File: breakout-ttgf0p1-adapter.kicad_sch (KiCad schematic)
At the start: 47 parts, among them J1 Conn_01x12, J2 Conn_02x08_Odd_Even, J3 DF12NB-60DS-0.5V_51, J4 Conn_02x08_Odd_Even, J5 DF12NB-50DS-0.5V_51, J6 Conn_02x08_Odd_Even, J8 Conn_02x08_Odd_Even, U1 AP2112K-3.3, U2 AP2112K-3.3, U4 24LC02

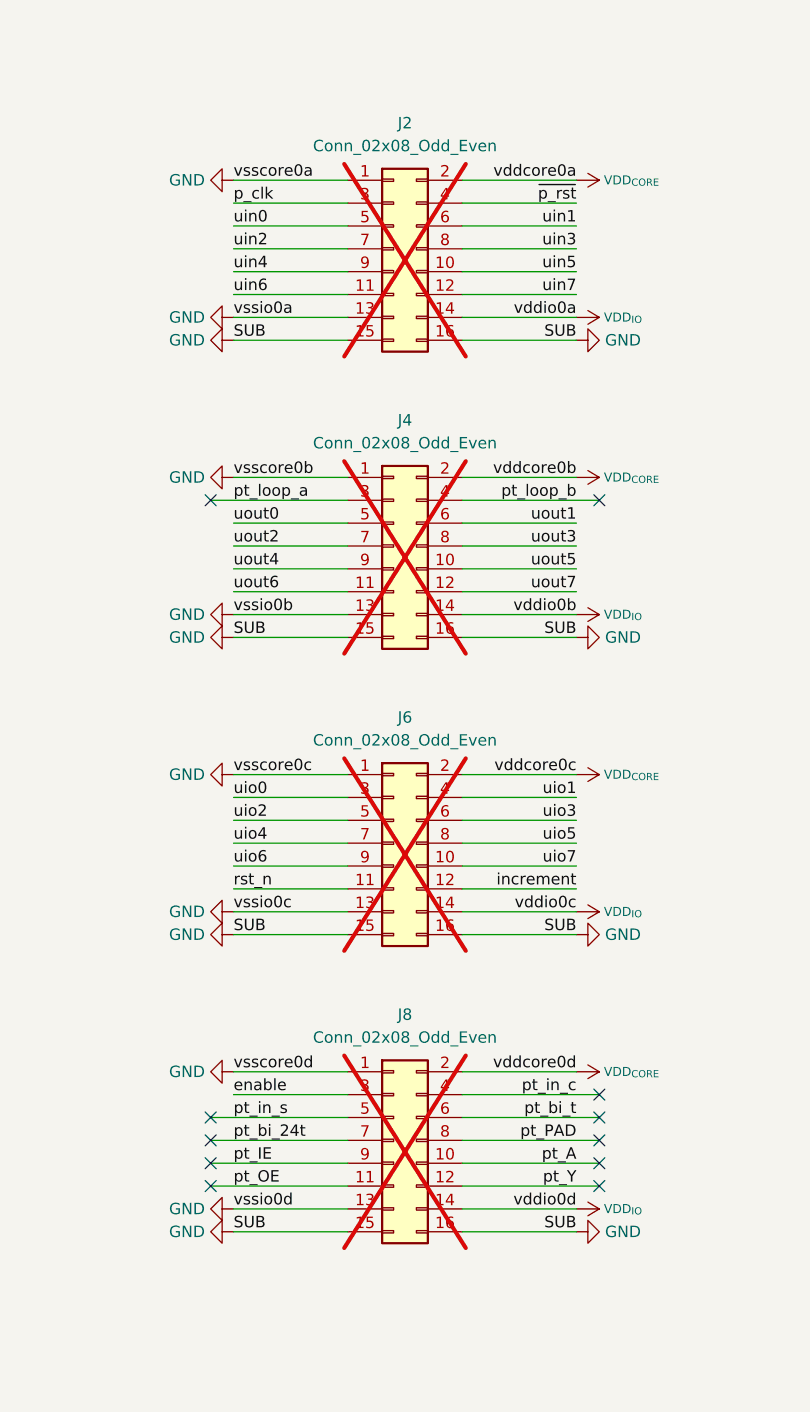
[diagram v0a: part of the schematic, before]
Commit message: replace THT headers with SMT ones & reroute
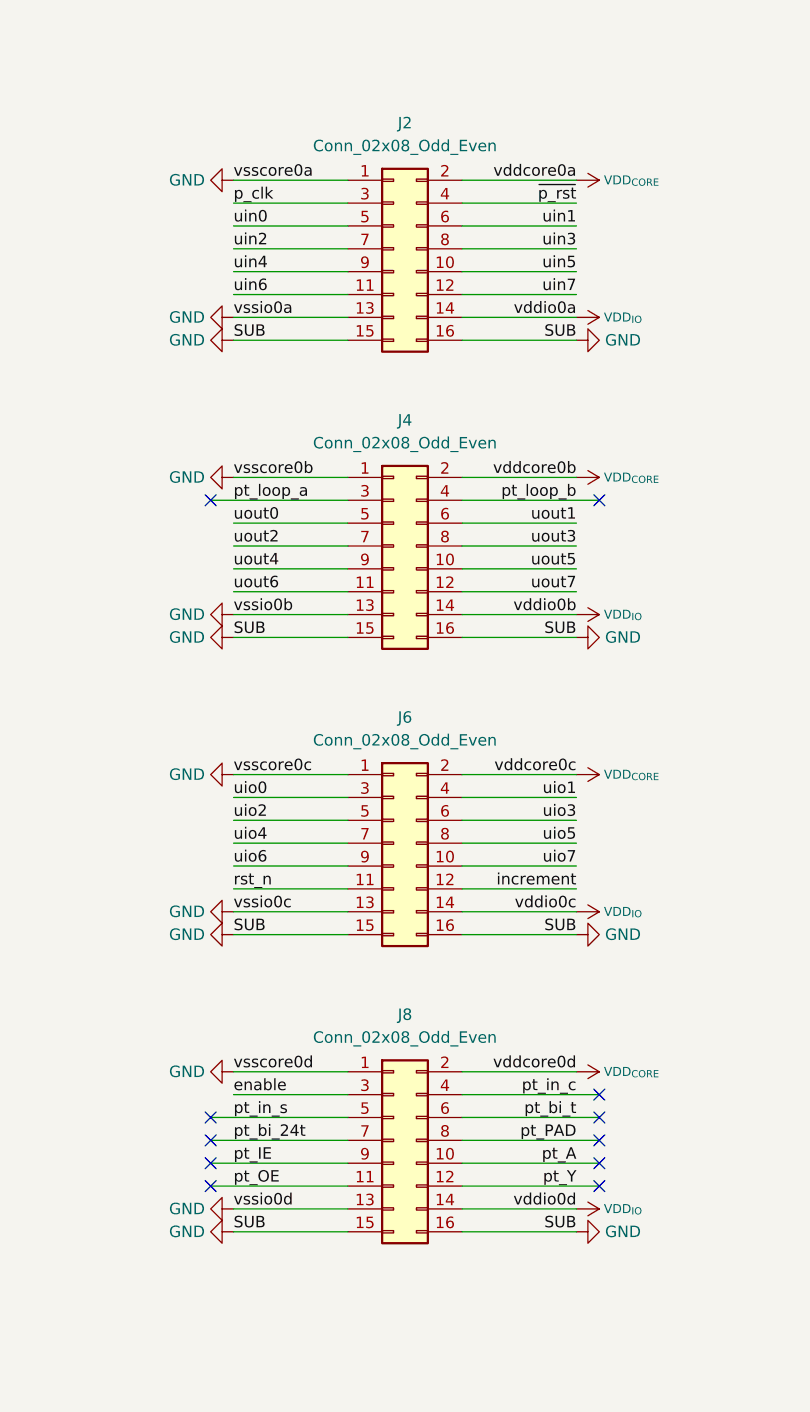
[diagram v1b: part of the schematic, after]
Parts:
- J2, J4, J6, J8: footprint Connector_PinHeader_2.54mm:PinHeader_2x08_P2.54mm_Vertical -> JLC2Kicad:HDR-SMD_16P-P2.54-V-F-R2-C8-LS7.2_H5.0; now fitted
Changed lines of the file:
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@@
 		(in_bom yes)
 		(on_board yes)
-		(dnp yes)
+		(dnp no)
 		(property "Reference" "J4"
 			(at 198.12 142.24 0)
@@
 			)
 		)
-		(property "Footprint" "Connector_PinHeader_2.54mm:PinHeader_2x08_P2.54mm_Vertical"
+		(property "Footprint" "JLC2Kicad:HDR-SMD_16P-P2.54-V-F-R2-C8-LS7.2_H5.0"
 			(at 196.85 156.21 0)
 			(effects
@@
 		(in_bom yes)
 		(on_board yes)
-		(dnp yes)
+		(dnp no)
 		(property "Reference" "J8"
 			(at 198.12 208.28 0)
@@
 			)
 		)
-		(property "Footprint" "Connector_PinHeader_2.54mm:PinHeader_2x08_P2.54mm_Vertical"
+		(property "Footprint" "JLC2Kicad:HDR-SMD_16P-P2.54-V-F-R2-C8-LS7.2_H5.0"
 			(at 196.85 222.25 0)
 			(effects
@@
 		(in_bom yes)
 		(on_board yes)
-		(dnp yes)
+		(dnp no)
 		(property "Reference" "J6"
 			(at 198.12 175.26 0)
@@
 			)
 		)
-		(property "Footprint" "Connector_PinHeader_2.54mm:PinHeader_2x08_P2.54mm_Vertical"
+		(property "Footprint" "JLC2Kicad:HDR-SMD_16P-P2.54-V-F-R2-C8-LS7.2_H5.0"
 			(at 196.85 189.23 0)
 			(effects
@@
 		(in_bom yes)
 		(on_board yes)
-		(dnp yes)
+		(dnp no)
 		(fields_autoplaced yes)
 		(property "Reference" "J2"
@@
 			)
 		)
-		(property "Footprint" "Connector_PinHeader_2.54mm:PinHeader_2x08_P2.54mm_Vertical"
+		(property "Footprint" "JLC2Kicad:HDR-SMD_16P-P2.54-V-F-R2-C8-LS7.2_H5.0"
 			(at 196.85 123.19 0)
 			(effects

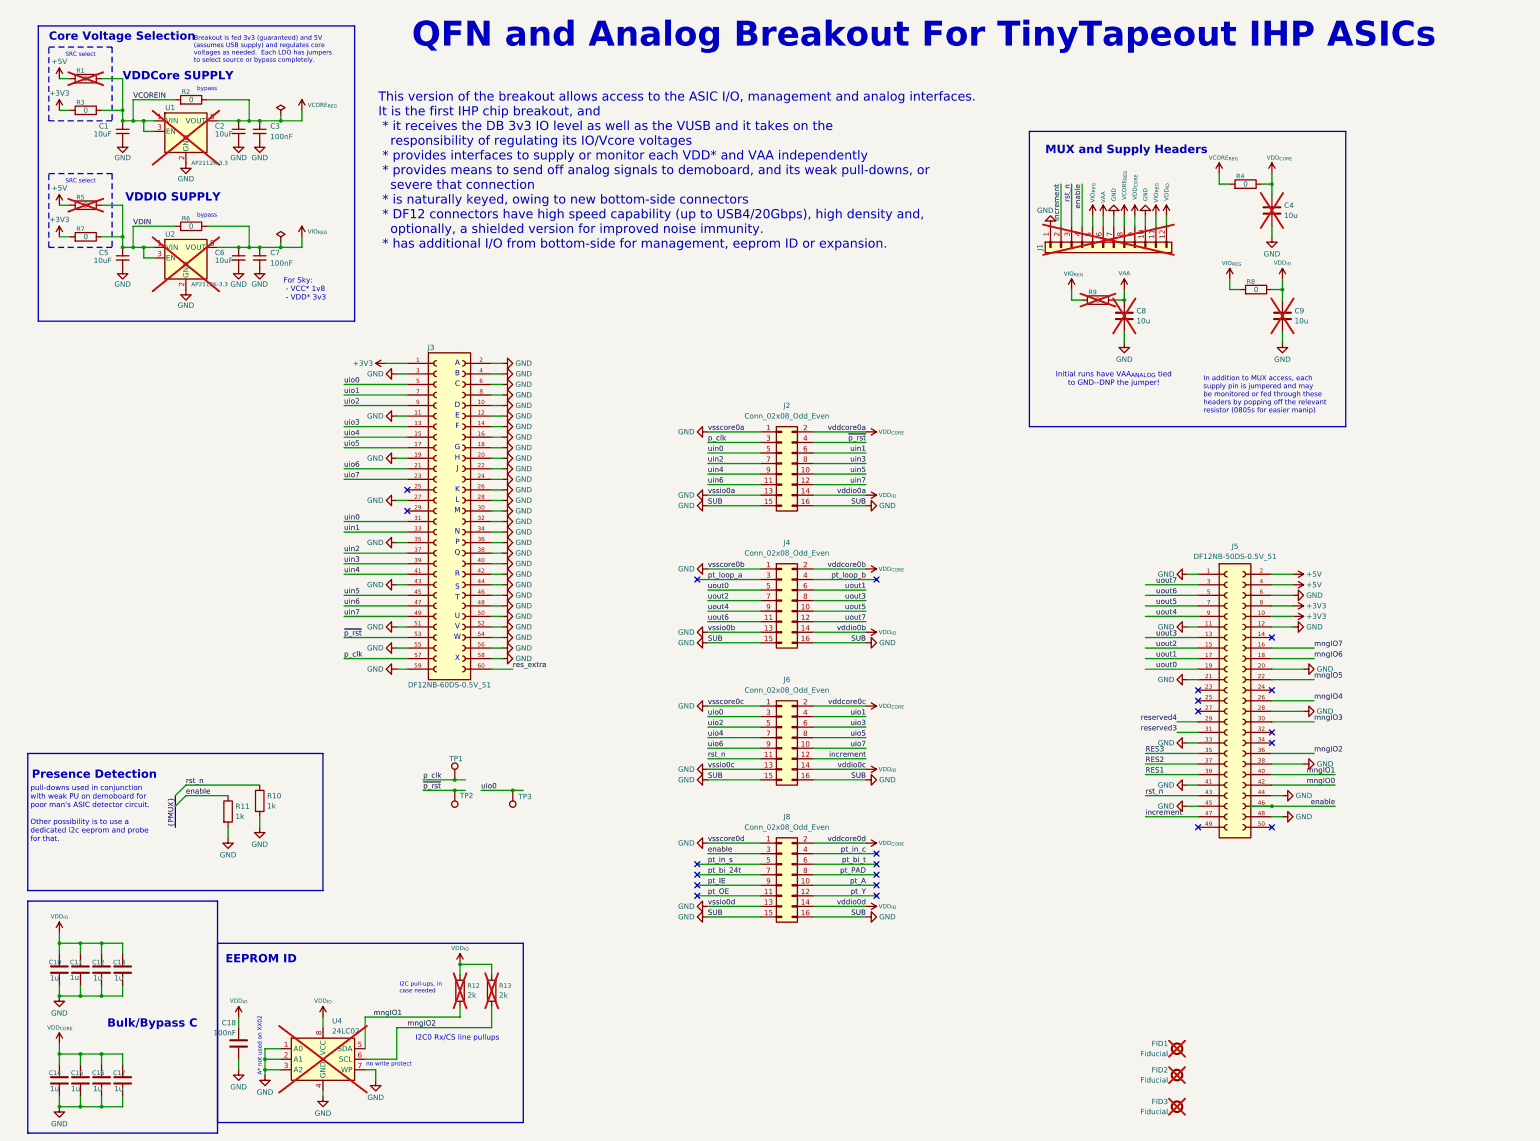
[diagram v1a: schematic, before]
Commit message: update component fields
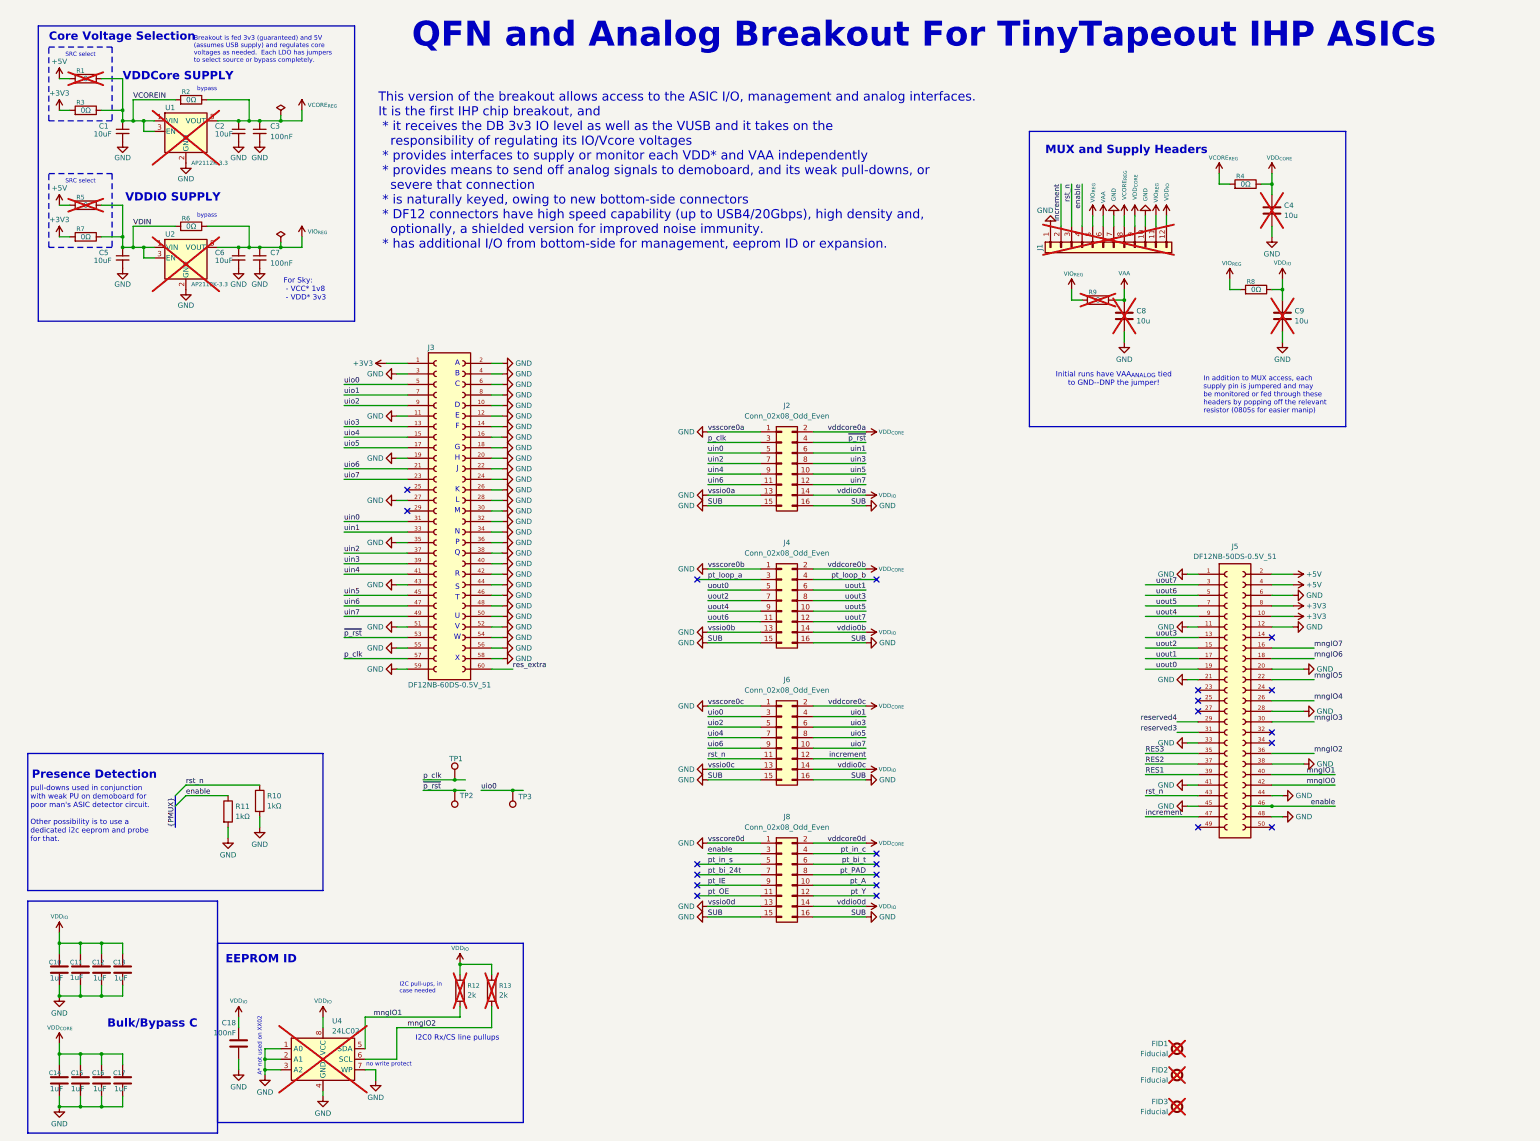
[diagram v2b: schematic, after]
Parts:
- C10, C11, C12, C13, C14, C15, C16, C17: value 1u -> 1uF
- R10, R11: value 1k -> 1kΩ
- R2: value 0 -> 0Ω; LCSC (none) -> C21189
- R3, R6, R7: value 0 -> 0Ω; LCSC C95177 -> C21189
- R4, R8: value 0 -> 0Ω; LCSC C4143065 -> C17477
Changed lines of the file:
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@@
 			)
 		)
-		(property "Value" "1u"
+		(property "Value" "1uF"
 			(at 20.574 247.142 0)
 			(effects
@@
 			)
 		)
-		(property "Value" "0"
+		(property "Value" "0Ω"
 			(at 308.61 55.88 90)
 			(effects
@@
 			)
 		)
-		(property "LCSC" "C4143065"
+		(property "LCSC" "C17477"
 			(at 304.8 55.88 0)
 			(show_name yes)
@@
 			)
 		)
-		(property "Value" "1k"
+		(property "Value" "1kΩ"
 			(at 72.898 205.6821 0)
 			(effects
@@
 			)
 		)
-		(property "Value" "0"
+		(property "Value" "0Ω"
 			(at 29.21 38.1 90)
 			(effects
@@
 			)
 		)
-		(property "LCSC" "C95177"
+		(property "LCSC" " C21189"
 			(at 25.4 38.1 0)
 			(show_name yes)
@@
 			)
 		)
-		(property "Value" "1u"
+		(property "Value" "1uF"
 			(at 30.988 247.142 0)
 			(effects
@@
 			)
 		)
-		(property "Value" "1u"
+		(property "Value" "1uF"
 			(at 25.4 247.015 0)
 			(effects
@@
 			)
 		)
-		(property "Value" "1u"
+		(property "Value" "1uF"
 			(at 30.988 273.812 0)
 			(effects
@@
 			)
 		)
-		(property "Value" "0"
+		(property "Value" "0Ω"
 			(at 311.15 81.28 90)
 			(effects
@@
 			)
 		)
-		(property "LCSC" "C4143065"
+		(property "LCSC" "C17477"
 			(at 307.34 81.28 0)
 			(show_name yes)
@@
 			)
 		)
-		(property "Value" "0"
+		(property "Value" "0Ω"
 			(at 54.61 66.04 90)
 			(effects
@@
 			)
 		)
-		(property "LCSC" "C95177"
+		(property "LCSC" " C21189"
 			(at 50.8 66.04 0)
 			(show_name yes)
@@
 			)
 		)
-		(property "Value" "1u"
+		(property "Value" "1uF"
 			(at 36.068 247.142 0)
 			(effects
@@
 			)
 		)
-		(property "Value" "1u"
+		(property "Value" "1uF"
 			(at 36.068 273.812 0)
 			(effects
@@
 			)
 		)
-		(property "Value" "0"
+		(property "Value" "0Ω"
 			(at 54.61 35.56 90)
 			(effects
@@
 			)
 		)
-		(property "LCSC" ""
+		(property "LCSC" " C21189"
 			(at 50.8 35.56 0)
 			(show_name yes)
@@
 			)
 		)
-		(property "Value" "0"
+		(property "Value" "0Ω"
 			(at 29.21 68.58 90)
 			(effects
@@
 			)
 		)
-		(property "LCSC" "C95177"
+		(property "LCSC" " C21189"
 			(at 25.4 68.58 0)
 			(show_name yes)
@@
 			)
 		)
-		(property "Value" "1u"
+		(property "Value" "1uF"
 			(at 20.574 273.812 0)
 			(effects
@@
 			)
 		)
-		(property "Value" "1u"
+		(property "Value" "1uF"
 			(at 25.654 273.812 0)
 			(effects
@@
 			)
 		)
-		(property "Value" "1k"
+		(property "Value" "1kΩ"
 			(at 65.278 208.2221 0)
 			(effects
